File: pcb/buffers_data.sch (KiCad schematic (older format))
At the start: 8 parts, among them U1 74LVCH162245A, U2 74LVCH162245A

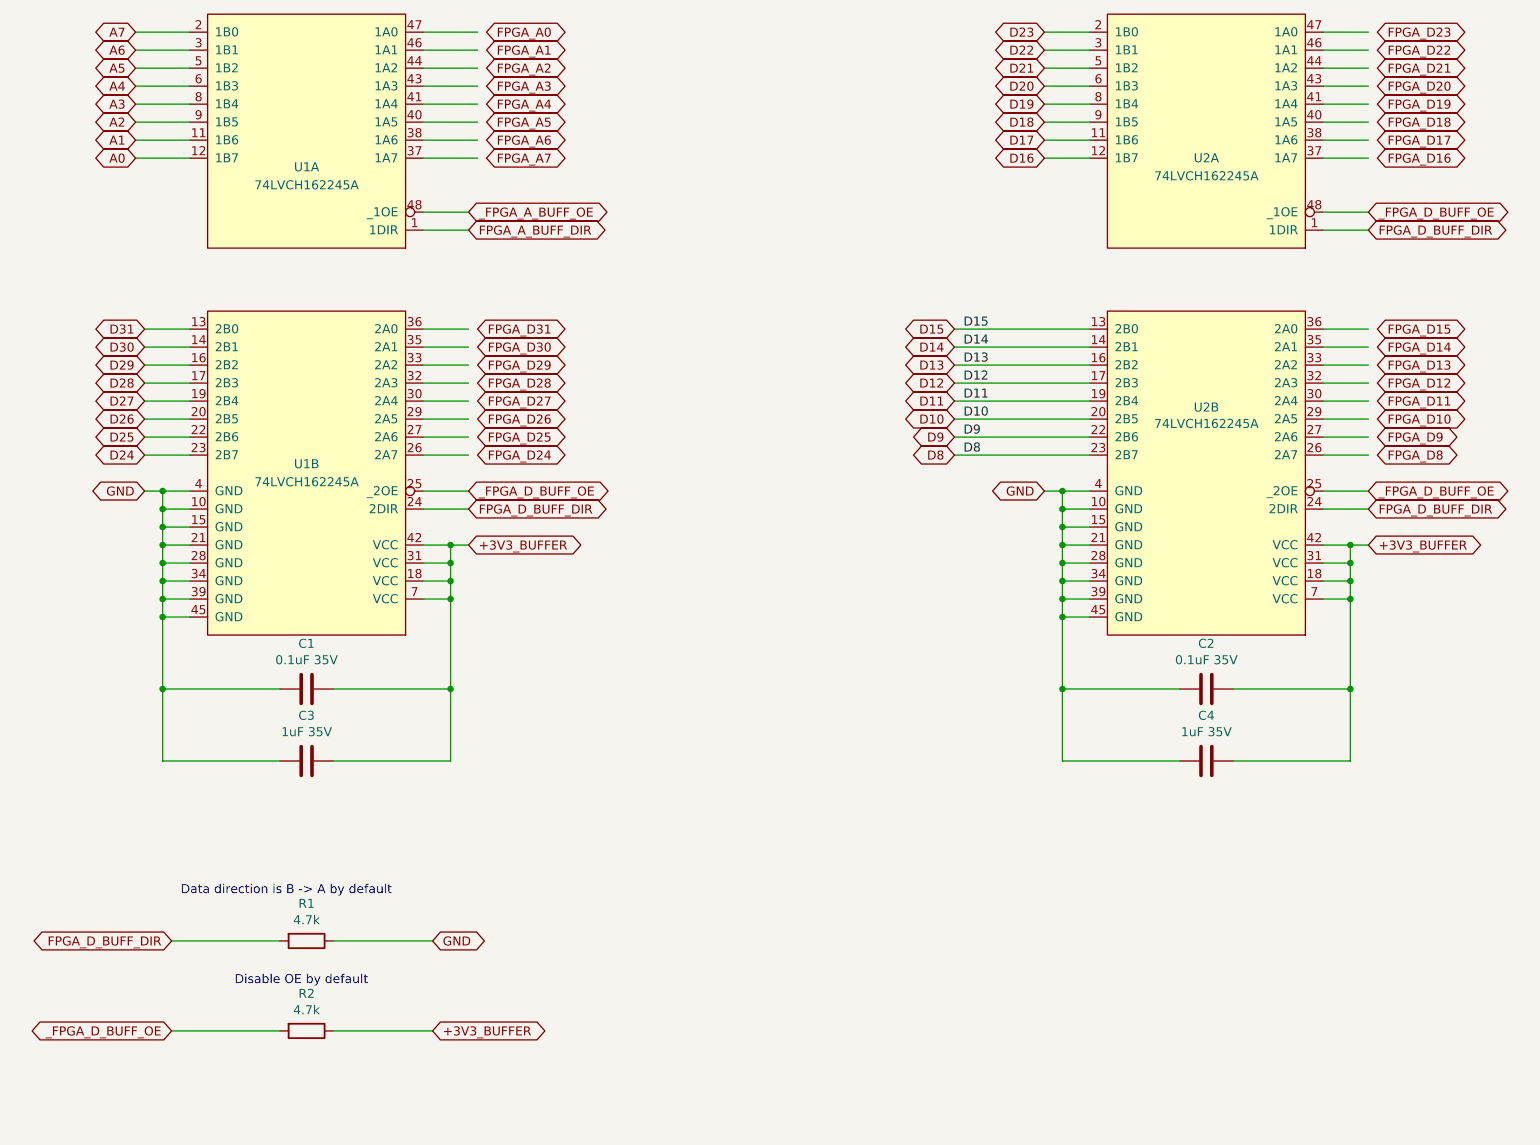
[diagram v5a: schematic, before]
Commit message: Buffers power scheme rework in progress, re-annotate board
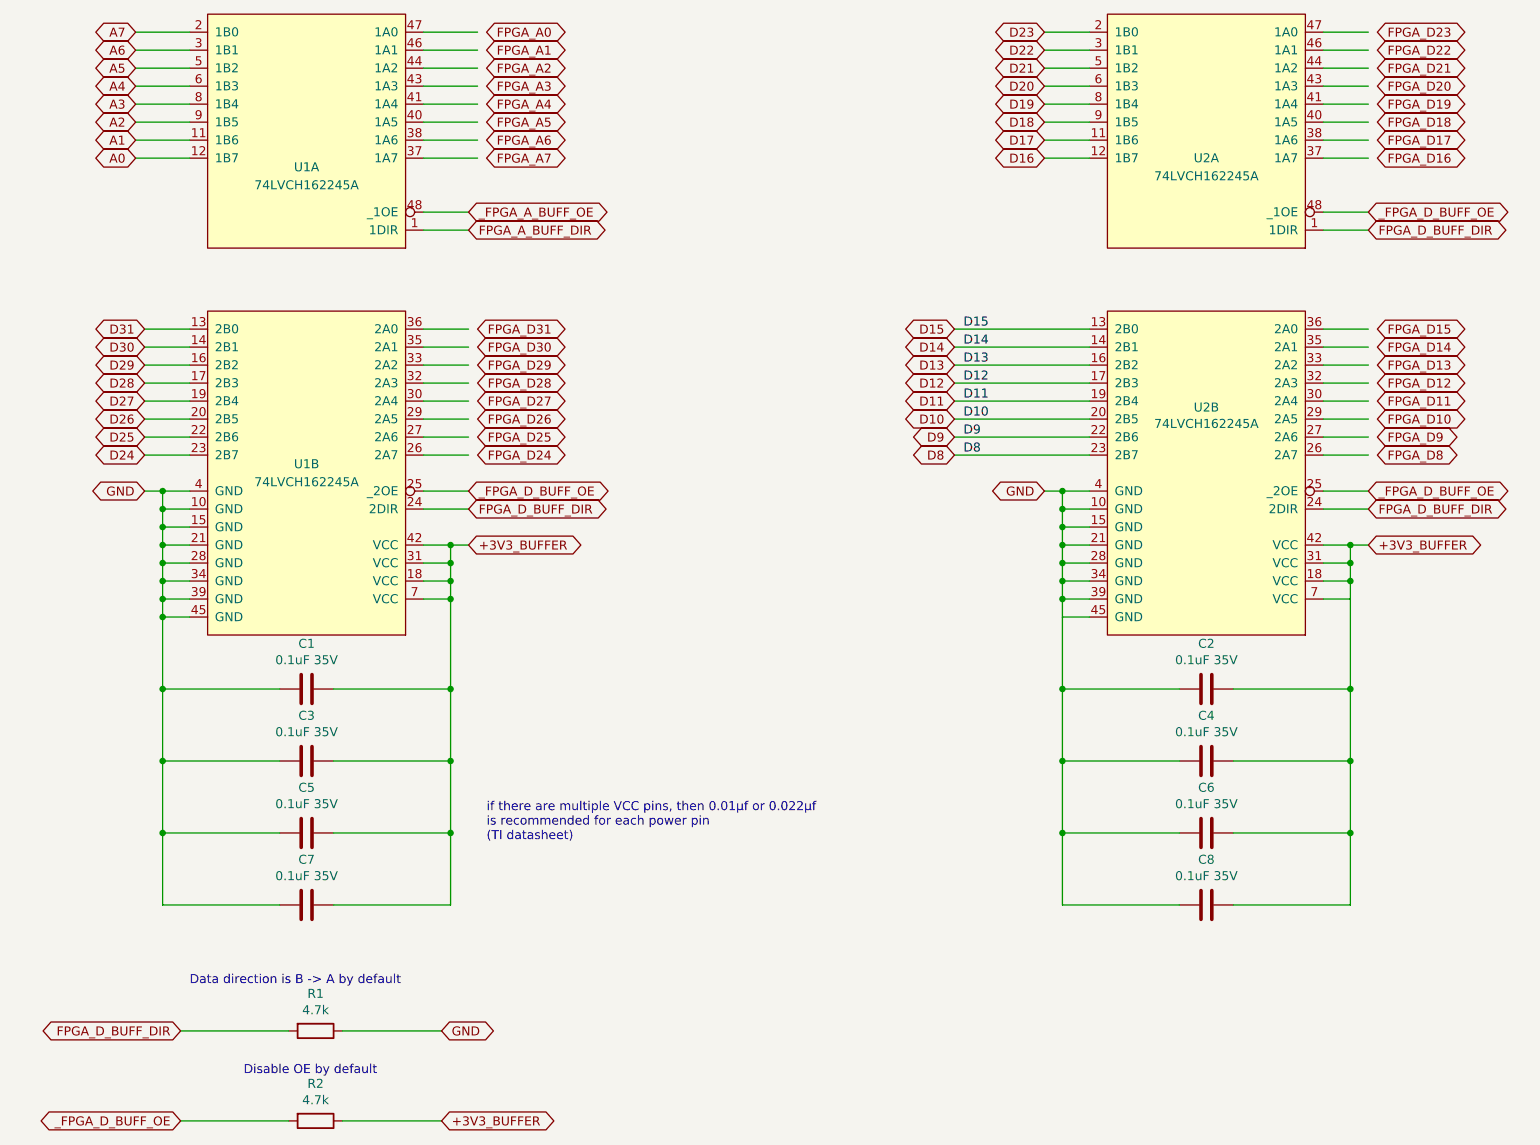
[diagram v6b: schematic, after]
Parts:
- added C5, C6, C7, C8: 0.1uF 35V, Capacitor_SMD:C_0603_1608Metric_Pad1.05x0.95mm_HandSolder, symbol Device:C
- C3, C4: value 1uF 35V -> 0.1uF 35V; footprint Capacitor_SMD:C_0805_2012Metric_Pad1.15x1.40mm_HandSolder -> Capacitor_SMD:C_0603_1608Metric_Pad1.05x0.95mm_HandSolder
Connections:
- wire segments 140 -> 156
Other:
- note added: "if there are multiple VCC pins, then 0.01μf or 0.022μf\nis recommended for each power pin\n(TI datasheet)"
- moved on the sheet: R1, R2
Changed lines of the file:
@@
 	8900 4600 9050 4600
-$Comp
-L Device:C C3
-U 1 1 5E91F423
-P 3250 5600
-F 0 "C3" V 3502 5600 50  0000 C CNN
-F 1 "1uF 35V" V 3411 5600 50  0000 C CNN
-F 2 "Capacitor_SMD:C_0805_2012Metric_Pad1.15x1.40mm_HandSolder" H 3288 5450 50  0001 C CNN
-F 3 "~" H 3250 5600 50  0001 C CNN
-	1    3250 5600
-	0    -1   -1   0
-$EndComp
 $Comp
 L Device:C C1
@@
 	0    -1   -1   0
 $EndComp
-$Comp
-L Device:C C4
-U 1 1 5E91F426
-P 8250 5600
-F 0 "C4" V 8502 5600 50  0000 C CNN
-F 1 "1uF 35V" V 8411 5600 50  0000 C CNN
-F 2 "Capacitor_SMD:C_0805_2012Metric_Pad1.15x1.40mm_HandSolder" H 8288 5450 50  0001 C CNN
-F 3 "~" H 8250 5600 50  0001 C CNN
-	1    8250 5600
-	0    -1   -1   0
-$EndComp
-$Comp
-L Device:C C2
-U 1 1 5E79CB2C
-P 8250 5200
-F 0 "C2" V 8502 5200 50  0000 C CNN
-F 1 "0.1uF 35V" V 8411 5200 50  0000 C CNN
-F 2 "Capacitor_SMD:C_0603_1608Metric_Pad1.05x0.95mm_HandSolder" H 8288 5050 50  0001 C CNN
-F 3 "~" H 8250 5200 50  0001 C CNN
-	1    8250 5200
-	0    -1   -1   0
-$EndComp
-Wire Wire Line
-	3100 5600 2450 5600
 Wire Wire Line
 	3400 5200 4050 5200
-Wire Wire Line
-	8100 5600 7450 5600
-Wire Wire Line
-	8400 5200 9050 5200
 Text Label 6900 3200 0    50   ~ 0
 D15
@@
 L Device:R R1
 U 1 1 5E7D2869
-P 3250 6600
-F 0 "R1" V 3043 6600 50  0000 C CNN
-F 1 "4.7k" V 3134 6600 50  0000 C CNN
-F 2 "Resistor_SMD:R_0603_1608Metric_Pad1.05x0.95mm_HandSolder" V 3180 6600 50  0001 C CNN
-F 3 "~" H 3250 6600 50  0001 C CNN
-	1    3250 6600
+P 3300 7100
+F 0 "R1" V 3093 7100 50  0000 C CNN
+F 1 "4.7k" V 3184 7100 50  0000 C CNN
+F 2 "Resistor_SMD:R_0603_1608Metric_Pad1.05x0.95mm_HandSolder" V 3230 7100 50  0001 C CNN
+F 3 "~" H 3300 7100 50  0001 C CNN
+	1    3300 7100
 	0    1    1    0
 $EndComp
@@
 L Device:R R2
 U 1 1 5E7D396E
-P 3250 7100
-F 0 "R2" V 3043 7100 50  0000 C CNN
-F 1 "4.7k" V 3134 7100 50  0000 C CNN
-F 2 "Resistor_SMD:R_0603_1608Metric_Pad1.05x0.95mm_HandSolder" V 3180 7100 50  0001 C CNN
-F 3 "~" H 3250 7100 50  0001 C CNN
-	1    3250 7100
+P 3300 7600
+F 0 "R2" V 3093 7600 50  0000 C CNN
+F 1 "4.7k" V 3184 7600 50  0000 C CNN
+F 2 "Resistor_SMD:R_0603_1608Metric_Pad1.05x0.95mm_HandSolder" V 3230 7600 50  0001 C CNN
+F 3 "~" H 3300 7600 50  0001 C CNN
+	1    3300 7600
 	0    1    1    0
 $EndComp
 Wire Wire Line
-	2500 6600 3100 6600
-Wire Wire Line
-	3100 7100 2500 7100
-Wire Wire Line
-	3400 6600 3950 6600
-Wire Wire Line
-	3950 7100 3400 7100
-Text Notes 2850 6850 0    50   ~ 0
+	2550 7100 3150 7100
+Wire Wire Line
+	3150 7600 2550 7600
+Wire Wire Line
+	3450 7100 4000 7100
+Wire Wire Line
+	4000 7600 3450 7600
+Text Notes 2900 7350 0    50   ~ 0
 Disable OE by default
-Text Notes 2550 6350 0    50   ~ 0
+Text Notes 2600 6850 0    50   ~ 0
 Data direction is B -> A by default
 Text GLabel 2350 3200 0    50   BiDi ~ 0
@@
 	4050 5200 4050 5600
 Wire Wire Line
-	4050 5600 3400 5600
-Wire Wire Line
 	2450 5200 2450 5600
-Wire Wire Line
-	7450 4800 7450 5200
-Connection ~ 7450 4800
-Connection ~ 7450 5200
-Wire Wire Line
-	7450 5200 8100 5200
-Wire Wire Line
-	7450 5200 7450 5600
-Wire Wire Line
-	9050 4700 9050 5200
-Connection ~ 9050 4700
-Connection ~ 9050 5200
-Wire Wire Line
-	9050 5200 9050 5600
-Wire Wire Line
-	9050 5600 8400 5600
-Text GLabel 3950 7100 2    50   BiDi ~ 0
+Text GLabel 4000 7600 2    50   BiDi ~ 0
 +3V3_BUFFER
-Text GLabel 2500 6600 0    50   BiDi ~ 0
+Text GLabel 2550 7100 0    50   BiDi ~ 0
 FPGA_D_BUFF_DIR
-Text GLabel 2500 7100 0    50   BiDi ~ 0
+Text GLabel 2550 7600 0    50   BiDi ~ 0
 _FPGA_D_BUFF_OE
-Text GLabel 3950 6600 2    50   BiDi ~ 0
+Text GLabel 4000 7100 2    50   BiDi ~ 0
 GND
 Text GLabel 9150 4100 2    50   BiDi ~ 0
@@
 Text GLabel 4150 2550 2    50   BiDi ~ 0
 _FPGA_A_BUFF_OE
+$Comp
+L Device:C C3
+U 1 1 5E765D5F
+P 3250 5600
+F 0 "C3" V 3502 5600 50  0000 C CNN
+F 1 "0.1uF 35V" V 3411 5600 50  0000 C CNN
+F 2 "Capacitor_SMD:C_0603_1608Metric_Pad1.05x0.95mm_HandSolder" H 3288 5450 50  0001 C CNN
+F 3 "~" H 3250 5600 50  0001 C CNN
+	1    3250 5600
+	0    -1   -1   0
+$EndComp
+Wire Wire Line
+	3400 5600 4050 5600
+Wire Wire Line
+	2450 5600 3100 5600
+$Comp
+L Device:C C5
+U 1 1 5E76DAF4
+P 3250 6000
+F 0 "C5" V 3502 6000 50  0000 C CNN
+F 1 "0.1uF 35V" V 3411 6000 50  0000 C CNN
+F 2 "Capacitor_SMD:C_0603_1608Metric_Pad1.05x0.95mm_HandSolder" H 3288 5850 50  0001 C CNN
+F 3 "~" H 3250 6000 50  0001 C CNN
+	1    3250 6000
+	0    -1   -1   0
+$EndComp
+Wire Wire Line
+	3400 6000 4050 6000
+Wire Wire Line
+	2450 6000 3100 6000
+$Comp
+L Device:C C7
+U 1 1 5E783C2B
+P 3250 6400
+F 0 "C7" V 3502 6400 50  0000 C CNN
+F 1 "0.1uF 35V" V 3411 6400 50  0000 C CNN
+F 2 "Capacitor_SMD:C_0603_1608Metric_Pad1.05x0.95mm_HandSolder" H 3288 6250 50  0001 C CNN
+F 3 "~" H 3250 6400 50  0001 C CNN
+	1    3250 6400
+	0    -1   -1   0
+$EndComp
+Wire Wire Line
+	3400 6400 4050 6400
+Wire Wire Line
+	2450 6400 3100 6400
+Wire Wire Line
+	2450 6000 2450 5600
+Connection ~ 2450 5600
+Wire Wire Line
+	2450 6400 2450 6000
+Connection ~ 2450 6000
+Wire Wire Line
+	4050 6400 4050 6000
+Wire Wire Line
+	4050 6000 4050 5600
+Connection ~ 4050 6000
+Connection ~ 4050 5600
+Text Notes 4250 6050 0    50   ~ 0
+if there are multiple VCC pins, then 0.01μf or 0.022μf\nis recommended for each power pin\n(TI datasheet)
+$Comp
+L Device:C C2
+U 1 1 5E7C09E0
+P 8250 5200
+F 0 "C2" V 8502 5200 50  0000 C CNN
+F 1 "0.1uF 35V" V 8411 5200 50  0000 C CNN
+F 2 "Capacitor_SMD:C_0603_1608Metric_Pad1.05x0.95mm_HandSolder" H 8288 5050 50  0001 C CNN
+F 3 "~" H 8250 5200 50  0001 C CNN
+	1    8250 5200
+	0    -1   -1   0
+$EndComp
+Wire Wire Line
+	8400 5200 9050 5200
+Wire Wire Line
+	7450 4800 7450 5200
+Connection ~ 7450 5200
+Wire Wire Line
+	7450 5200 8100 5200
+Wire Wire Line
+	9050 4700 9050 5200
+Connection ~ 9050 5200
+Wire Wire Line
+	9050 5200 9050 5600
+Wire Wire Line
+	7450 5200 7450 5600
+$Comp
+L Device:C C4
+U 1 1 5E7C09EE
+P 8250 5600
+F 0 "C4" V 8502 5600 50  0000 C CNN
+F 1 "0.1uF 35V" V 8411 5600 50  0000 C CNN
+F 2 "Capacitor_SMD:C_0603_1608Metric_Pad1.05x0.95mm_HandSolder" H 8288 5450 50  0001 C CNN
+F 3 "~" H 8250 5600 50  0001 C CNN
+	1    8250 5600
+	0    -1   -1   0
+$EndComp
+Wire Wire Line
+	8400 5600 9050 5600
+Wire Wire Line
+	7450 5600 8100 5600
+$Comp
+L Device:C C6
+U 1 1 5E7C09F6
+P 8250 6000
+F 0 "C6" V 8502 6000 50  0000 C CNN
+F 1 "0.1uF 35V" V 8411 6000 50  0000 C CNN
+F 2 "Capacitor_SMD:C_0603_1608Metric_Pad1.05x0.95mm_HandSolder" H 8288 5850 50  0001 C CNN
+F 3 "~" H 8250 6000 50  0001 C CNN
+	1    8250 6000
+	0    -1   -1   0
+$EndComp
+Wire Wire Line
+	8400 6000 9050 6000
+Wire Wire Line
+	7450 6000 8100 6000
+$Comp
+L Device:C C8
+U 1 1 5E7C09FE
+P 8250 6400
+F 0 "C8" V 8502 6400 50  0000 C CNN
+F 1 "0.1uF 35V" V 8411 6400 50  0000 C CNN
+F 2 "Capacitor_SMD:C_0603_1608Metric_Pad1.05x0.95mm_HandSolder" H 8288 6250 50  0001 C CNN
+F 3 "~" H 8250 6400 50  0001 C CNN
+	1    8250 6400
+	0    -1   -1   0
+$EndComp
+Wire Wire Line
+	8400 6400 9050 6400
+Wire Wire Line
+	7450 6400 8100 6400
+Wire Wire Line
+	7450 6000 7450 5600
+Connection ~ 7450 5600
+Wire Wire Line
+	7450 6400 7450 6000
+Connection ~ 7450 6000
+Wire Wire Line
+	9050 6400 9050 6000
+Wire Wire Line
+	9050 6000 9050 5600
+Connection ~ 9050 6000
+Connection ~ 9050 5600
 $EndSCHEMATC

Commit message: Some work done, sync
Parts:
- C1, C2, C3, C4, C5, C6, C7, C8: footprint Capacitor_SMD:C_0603_1608Metric_Pad1.05x0.95mm_HandSolder -> Capacitor_SMD:C_0402_1005Metric
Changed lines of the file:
@@
 F 0 "C1" V 3502 5200 50  0000 C CNN
 F 1 "0.1uF 35V" V 3411 5200 50  0000 C CNN
-F 2 "Capacitor_SMD:C_0603_1608Metric_Pad1.05x0.95mm_HandSolder" H 3288 5050 50  0001 C CNN
+F 2 "Capacitor_SMD:C_0402_1005Metric" H 3288 5050 50  0001 C CNN
 F 3 "~" H 3250 5200 50  0001 C CNN
 	1    3250 5200
@@
 F 0 "C3" V 3502 5600 50  0000 C CNN
 F 1 "0.1uF 35V" V 3411 5600 50  0000 C CNN
-F 2 "Capacitor_SMD:C_0603_1608Metric_Pad1.05x0.95mm_HandSolder" H 3288 5450 50  0001 C CNN
+F 2 "Capacitor_SMD:C_0402_1005Metric" H 3288 5450 50  0001 C CNN
 F 3 "~" H 3250 5600 50  0001 C CNN
 	1    3250 5600
@@
 F 0 "C5" V 3502 6000 50  0000 C CNN
 F 1 "0.1uF 35V" V 3411 6000 50  0000 C CNN
-F 2 "Capacitor_SMD:C_0603_1608Metric_Pad1.05x0.95mm_HandSolder" H 3288 5850 50  0001 C CNN
+F 2 "Capacitor_SMD:C_0402_1005Metric" H 3288 5850 50  0001 C CNN
 F 3 "~" H 3250 6000 50  0001 C CNN
 	1    3250 6000
@@
 F 0 "C7" V 3502 6400 50  0000 C CNN
 F 1 "0.1uF 35V" V 3411 6400 50  0000 C CNN
-F 2 "Capacitor_SMD:C_0603_1608Metric_Pad1.05x0.95mm_HandSolder" H 3288 6250 50  0001 C CNN
+F 2 "Capacitor_SMD:C_0402_1005Metric" H 3288 6250 50  0001 C CNN
 F 3 "~" H 3250 6400 50  0001 C CNN
 	1    3250 6400
@@
 F 0 "C2" V 8502 5200 50  0000 C CNN
 F 1 "0.1uF 35V" V 8411 5200 50  0000 C CNN
-F 2 "Capacitor_SMD:C_0603_1608Metric_Pad1.05x0.95mm_HandSolder" H 8288 5050 50  0001 C CNN
+F 2 "Capacitor_SMD:C_0402_1005Metric" H 8288 5050 50  0001 C CNN
 F 3 "~" H 8250 5200 50  0001 C CNN
 	1    8250 5200
@@
 F 0 "C4" V 8502 5600 50  0000 C CNN
 F 1 "0.1uF 35V" V 8411 5600 50  0000 C CNN
-F 2 "Capacitor_SMD:C_0603_1608Metric_Pad1.05x0.95mm_HandSolder" H 8288 5450 50  0001 C CNN
+F 2 "Capacitor_SMD:C_0402_1005Metric" H 8288 5450 50  0001 C CNN
 F 3 "~" H 8250 5600 50  0001 C CNN
 	1    8250 5600
@@
 F 0 "C6" V 8502 6000 50  0000 C CNN
 F 1 "0.1uF 35V" V 8411 6000 50  0000 C CNN
-F 2 "Capacitor_SMD:C_0603_1608Metric_Pad1.05x0.95mm_HandSolder" H 8288 5850 50  0001 C CNN
+F 2 "Capacitor_SMD:C_0402_1005Metric" H 8288 5850 50  0001 C CNN
 F 3 "~" H 8250 6000 50  0001 C CNN
 	1    8250 6000
@@
 F 0 "C8" V 8502 6400 50  0000 C CNN
 F 1 "0.1uF 35V" V 8411 6400 50  0000 C CNN
-F 2 "Capacitor_SMD:C_0603_1608Metric_Pad1.05x0.95mm_HandSolder" H 8288 6250 50  0001 C CNN
+F 2 "Capacitor_SMD:C_0402_1005Metric" H 8288 6250 50  0001 C CNN
 F 3 "~" H 8250 6400 50  0001 C CNN
 	1    8250 6400

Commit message: some dirty routing
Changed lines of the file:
@@
 Text GLabel 9150 4200 2    50   BiDi ~ 0
 FPGA_D_BUFF_DIR
-Text GLabel 9200 1550 2    50   BiDi ~ 0
+Text GLabel 9150 1550 2    50   BiDi ~ 0
 FPGA_D23
-Text GLabel 9200 1650 2    50   BiDi ~ 0
+Text GLabel 9150 1650 2    50   BiDi ~ 0
 FPGA_D22
-Text GLabel 9200 1750 2    50   BiDi ~ 0
+Text GLabel 9150 1750 2    50   BiDi ~ 0
 FPGA_D21
-Text GLabel 9200 1850 2    50   BiDi ~ 0
+Text GLabel 9150 1850 2    50   BiDi ~ 0
 FPGA_D20
-Text GLabel 9200 1950 2    50   BiDi ~ 0
+Text GLabel 9150 1950 2    50   BiDi ~ 0
 FPGA_D19
-Text GLabel 9200 2050 2    50   BiDi ~ 0
+Text GLabel 9150 2050 2    50   BiDi ~ 0
 FPGA_D18
-Text GLabel 9200 2150 2    50   BiDi ~ 0
+Text GLabel 9150 2150 2    50   BiDi ~ 0
 FPGA_D17
-Text GLabel 9200 2250 2    50   BiDi ~ 0
+Text GLabel 9150 2250 2    50   BiDi ~ 0
 FPGA_D16
-Text GLabel 9200 3200 2    50   BiDi ~ 0
+Text GLabel 9150 3200 2    50   BiDi ~ 0
 FPGA_D15
-Text GLabel 9200 3300 2    50   BiDi ~ 0
+Text GLabel 9150 3300 2    50   BiDi ~ 0
 FPGA_D14
-Text GLabel 9200 3400 2    50   BiDi ~ 0
+Text GLabel 9150 3400 2    50   BiDi ~ 0
 FPGA_D13
-Text GLabel 9200 3500 2    50   BiDi ~ 0
+Text GLabel 9150 3500 2    50   BiDi ~ 0
 FPGA_D12
-Text GLabel 9200 3600 2    50   BiDi ~ 0
+Text GLabel 9150 3600 2    50   BiDi ~ 0
 FPGA_D11
-Text GLabel 9200 3700 2    50   BiDi ~ 0
+Text GLabel 9150 3700 2    50   BiDi ~ 0
 FPGA_D10
-Text GLabel 9200 3800 2    50   BiDi ~ 0
+Text GLabel 9150 3800 2    50   BiDi ~ 0
 FPGA_D9
-Text GLabel 9200 3900 2    50   BiDi ~ 0
+Text GLabel 9150 3900 2    50   BiDi ~ 0
 FPGA_D8
 Wire Wire Line
@@
 Wire Wire Line
 	4150 4100 3900 4100
-Text GLabel 4200 3900 2    50   BiDi ~ 0
+Text GLabel 4150 3900 2    50   BiDi ~ 0
 FPGA_D24
-Text GLabel 4200 3800 2    50   BiDi ~ 0
+Text GLabel 4150 3800 2    50   BiDi ~ 0
 FPGA_D25
-Text GLabel 4200 3700 2    50   BiDi ~ 0
+Text GLabel 4150 3700 2    50   BiDi ~ 0
 FPGA_D26
-Text GLabel 4200 3600 2    50   BiDi ~ 0
+Text GLabel 4150 3600 2    50   BiDi ~ 0
 FPGA_D27
-Text GLabel 4200 3500 2    50   BiDi ~ 0
+Text GLabel 4150 3500 2    50   BiDi ~ 0
 FPGA_D28
-Text GLabel 4200 3400 2    50   BiDi ~ 0
+Text GLabel 4150 3400 2    50   BiDi ~ 0
 FPGA_D29
-Text GLabel 4200 3300 2    50   BiDi ~ 0
+Text GLabel 4150 3300 2    50   BiDi ~ 0
 FPGA_D30
-Text GLabel 4200 3200 2    50   BiDi ~ 0
+Text GLabel 4150 3200 2    50   BiDi ~ 0
 FPGA_D31
 Text GLabel 4150 4200 2    50   BiDi ~ 0
@@
 Wire Wire Line
 	3900 3200 4150 3200
-Text GLabel 4250 1550 2    50   BiDi ~ 0
+Text GLabel 4200 2250 2    50   BiDi ~ 0
 FPGA_A0
-Text GLabel 4250 1650 2    50   BiDi ~ 0
+Text GLabel 4200 2150 2    50   BiDi ~ 0
 FPGA_A1
-Text GLabel 4250 1750 2    50   BiDi ~ 0
+Text GLabel 4200 2050 2    50   BiDi ~ 0
 FPGA_A2
-Text GLabel 4250 1850 2    50   BiDi ~ 0
+Text GLabel 4200 1950 2    50   BiDi ~ 0
 FPGA_A3
-Text GLabel 4250 1950 2    50   BiDi ~ 0
+Text GLabel 4200 1850 2    50   BiDi ~ 0
 FPGA_A4
-Text GLabel 4250 2050 2    50   BiDi ~ 0
+Text GLabel 4200 1750 2    50   BiDi ~ 0
 FPGA_A5
-Text GLabel 4250 2150 2    50   BiDi ~ 0
+Text GLabel 4200 1650 2    50   BiDi ~ 0
 FPGA_A6
-Text GLabel 4250 2250 2    50   BiDi ~ 0
+Text GLabel 4200 1550 2    50   BiDi ~ 0
 FPGA_A7
 Wire Wire Line
